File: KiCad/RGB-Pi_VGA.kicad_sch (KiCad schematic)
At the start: 39 parts, among them J1 Raspberry_Pi_4, J2 SCART-F, J3 DE15_Plug_HighDensity_Mountin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, J4 SJ1-3535NG, Q1 MMBT3904, U1 ST662A

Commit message: Change C8, C9 footprints from 1206 to 0805.
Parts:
- C8, C9: footprint Capacitor_SMD:C_1206_3216Metric_Pad1.33x1.80mm_HandSolder -> Resistor_SMD:R_0805_2012Metric_Pad1.20x1.40mm_HandSolder
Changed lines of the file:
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@@
 			)
 		)
-		(property "Footprint" "Capacitor_SMD:C_1206_3216Metric_Pad1.33x1.80mm_HandSolder"
+		(property "Footprint" "Resistor_SMD:R_0805_2012Metric_Pad1.20x1.40mm_HandSolder"
 			(at 228.6 200.9648 0)
 			(hide yes)
@@
 			)
 		)
-		(property "Footprint" "Capacitor_SMD:C_1206_3216Metric_Pad1.33x1.80mm_HandSolder"
+		(property "Footprint" "Resistor_SMD:R_0805_2012Metric_Pad1.20x1.40mm_HandSolder"
 			(at 228.6 195.8848 0)
 			(hide yes)

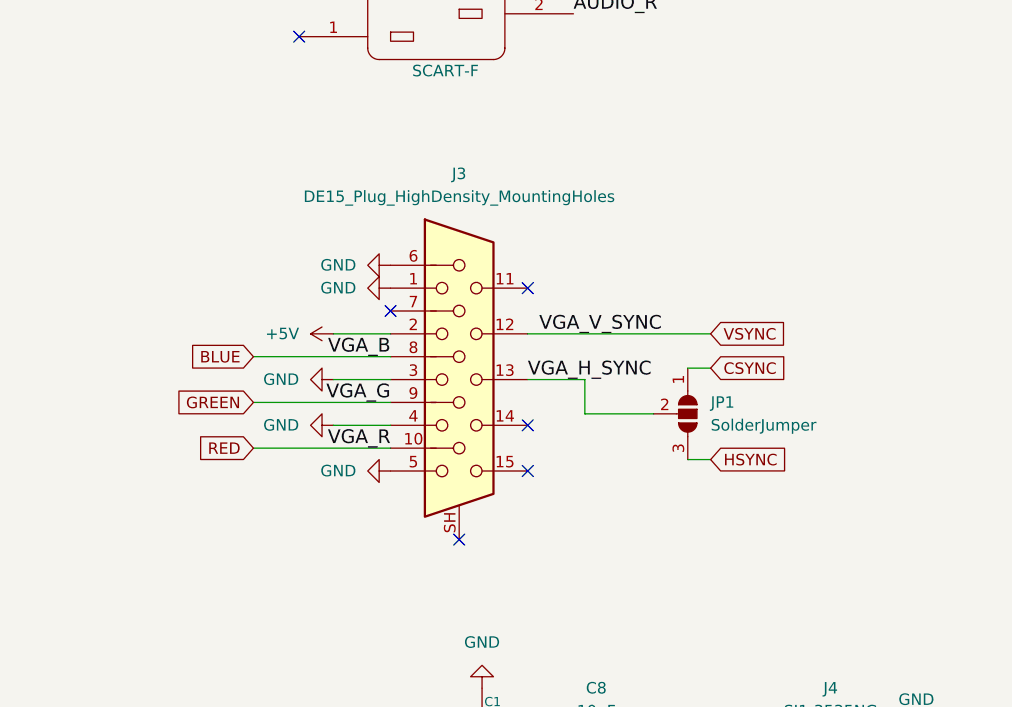
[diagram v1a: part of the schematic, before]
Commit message: Correct DE15/VGA connector pinout.
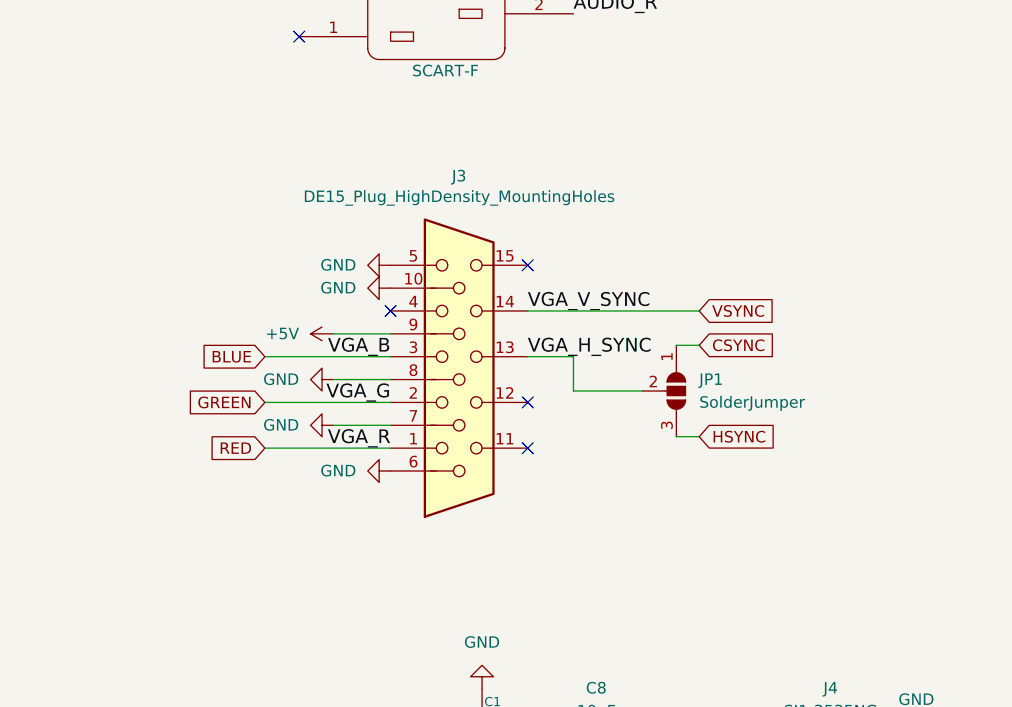
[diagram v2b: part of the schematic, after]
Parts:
- J3: symbol Connector:DE15_Socket_HighDensity_MountingHoles -> Connector:DE15_Socket_HighDensity
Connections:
- net +5V: now also J3.9; no longer J3.2
- net BLUE: now also J3.3; no longer J3.8
- net GND: now also J3.10, J3.7, J3.8; no longer J3.1, J3.3, J3.4
- net GREEN: now also J3.2; no longer J3.9
- net RED: now also J3.1; no longer J3.10
- net VSYNC: now also J3.14; no longer J3.12
- no-connect marks 26 -> 25
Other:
- moved on the sheet: JP1
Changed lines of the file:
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@@
 	)
 	(no_connect
-		(at 209.55 172.72)
-	)
-	(no_connect
 		(at 99.06 129.54)
 	)
@@
 	)
 	(no_connect
-		(at 217.17 144.78)
+		(at 217.17 142.24)
 	)
 	(no_connect
@@
 	)
 	(no_connect
-		(at 217.17 165.1)
+		(at 217.17 162.56)
 	)
 	(no_connect
-		(at 217.17 160.02)
+		(at 217.17 157.48)
 	)
 	(no_connect
@@
 	(wire
 		(pts
+			(xy 217.17 147.32) (xy 236.22 147.32)
+		)
+		(stroke
+			(width 0)
+			(type default)
+		)
+	)
+	(wire
+		(pts
 			(xy 260.35 195.58) (xy 257.81 195.58)
 		)
@@
 	(wire
 		(pts
+			(xy 187.96 152.4) (xy 201.93 152.4)
+		)
+		(stroke
+			(width 0)
+			(type default)
+		)
+	)
+	(wire
+		(pts
 			(xy 54.61 45.72) (xy 58.42 45.72)
 		)
@@
 	(wire
 		(pts
+			(xy 195.58 149.86) (xy 201.93 149.86)
+		)
+		(stroke
+			(width 0)
+			(type default)
+		)
+	)
+	(wire
+		(pts
 			(xy 101.6 41.91) (xy 114.3 41.91)
 		)
@@
 	(wire
 		(pts
+			(xy 187.96 157.48) (xy 201.93 157.48)
+		)
+		(stroke
+			(width 0)
+			(type default)
+		)
+	)
+	(wire
+		(pts
 			(xy 43.18 275.59) (xy 48.26 275.59)
 		)
@@
 	(wire
 		(pts
-			(xy 223.52 154.94) (xy 223.52 158.75)
+			(xy 222.25 152.4) (xy 222.25 156.21)
 		)
 		(stroke
@@
 	(wire
 		(pts
-			(xy 186.69 157.48) (xy 201.93 157.48)
-		)
-		(stroke
-			(width 0)
-			(type default)
-		)
-	)
-	(wire
-		(pts
 			(xy 27.94 182.88) (xy 27.94 184.15)
 		)
@@
 	(wire
 		(pts
-			(xy 237.49 163.83) (xy 234.95 163.83)
+			(xy 236.22 161.29) (xy 233.68 161.29)
 		)
 		(stroke
@@
 	(wire
 		(pts
-			(xy 195.58 160.02) (xy 201.93 160.02)
-		)
-		(stroke
-			(width 0)
-			(type default)
-		)
-	)
-	(wire
-		(pts
 			(xy 130.81 44.45) (xy 137.16 44.45)
 		)
@@
 	(wire
 		(pts
+			(xy 217.17 152.4) (xy 222.25 152.4)
+		)
+		(stroke
+			(width 0)
+			(type default)
+		)
+	)
+	(wire
+		(pts
 			(xy 27.94 228.6) (xy 35.56 228.6)
 		)
@@
 	(wire
 		(pts
-			(xy 195.58 149.86) (xy 201.93 149.86)
-		)
-		(stroke
-			(width 0)
-			(type default)
-		)
-	)
-	(wire
-		(pts
 			(xy 27.94 228.6) (xy 27.94 231.14)
 		)
@@
 	(wire
 		(pts
-			(xy 195.58 154.94) (xy 201.93 154.94)
-		)
-		(stroke
-			(width 0)
-			(type default)
-		)
-	)
-	(wire
-		(pts
 			(xy 176.53 81.28) (xy 191.77 81.28)
 		)
@@
 	(wire
 		(pts
-			(xy 186.69 162.56) (xy 201.93 162.56)
+			(xy 236.22 151.13) (xy 233.68 151.13)
 		)
 		(stroke
@@
 	(wire
 		(pts
-			(xy 237.49 153.67) (xy 234.95 153.67)
+			(xy 63.5 182.88) (xy 67.31 182.88)
 		)
 		(stroke
@@
 	(wire
 		(pts
-			(xy 63.5 182.88) (xy 67.31 182.88)
+			(xy 130.81 46.99) (xy 130.81 52.07)
 		)
 		(stroke
@@
 	(wire
 		(pts
-			(xy 130.81 46.99) (xy 130.81 52.07)
+			(xy 86.36 182.88) (xy 93.98 182.88)
 		)
 		(stroke
@@
 	(wire
 		(pts
-			(xy 86.36 182.88) (xy 93.98 182.88)
+			(xy 127 261.62) (xy 127 264.16)
 		)
 		(stroke
@@
 	(wire
 		(pts
-			(xy 127 261.62) (xy 127 264.16)
+			(xy 48.26 275.59) (xy 54.61 275.59)
 		)
 		(stroke
@@
 	(wire
 		(pts
-			(xy 48.26 275.59) (xy 54.61 275.59)
+			(xy 121.92 228.6) (xy 128.27 228.6)
 		)
 		(stroke
@@
 	(wire
 		(pts
-			(xy 121.92 228.6) (xy 128.27 228.6)
+			(xy 187.96 162.56) (xy 201.93 162.56)
 		)
 		(stroke
@@
 	(wire
 		(pts
-			(xy 186.69 152.4) (xy 201.93 152.4)
+			(xy 195.58 160.02) (xy 201.93 160.02)
 		)
 		(stroke
@@
 	(wire
 		(pts
-			(xy 217.17 154.94) (xy 223.52 154.94)
-		)
-		(stroke
-			(width 0)
-			(type default)
-		)
-	)
-	(wire
-		(pts
 			(xy 176.53 101.6) (xy 191.77 101.6)
 		)
@@
 	(wire
 		(pts
-			(xy 217.17 149.86) (xy 237.49 149.86)
+			(xy 222.25 156.21) (xy 229.87 156.21)
 		)
 		(stroke
@@
 	(wire
 		(pts
-			(xy 223.52 158.75) (xy 231.14 158.75)
+			(xy 27.94 168.91) (xy 27.94 171.45)
 		)
 		(stroke
@@
 	(wire
 		(pts
-			(xy 27.94 168.91) (xy 27.94 171.45)
+			(xy 43.18 31.75) (xy 54.61 31.75)
 		)
 		(stroke
@@
 	(wire
 		(pts
-			(xy 43.18 31.75) (xy 54.61 31.75)
+			(xy 113.03 52.07) (xy 101.6 52.07)
 		)
 		(stroke
@@
 	(wire
 		(pts
-			(xy 113.03 52.07) (xy 101.6 52.07)
+			(xy 195.58 154.94) (xy 201.93 154.94)
 		)
 		(stroke
@@
 	)
 	(label "VGA_H_SYNC"
-		(at 217.17 154.94 0)
+		(at 217.17 152.4 0)
 		(effects
 			(font
@@
 	)
 	(label "VGA_V_SYNC"
-		(at 218.44 149.86 0)
+		(at 217.17 147.32 0)
 		(effects
 			(font
@@
 	(global_label "RED"
 		(shape input)
-		(at 186.69 162.56 180)
+		(at 187.96 162.56 180)
 		(fields_autoplaced yes)
 		(effects
@@
 		)
 		(property "Intersheetrefs" "${INTERSHEET_REFS}"
-			(at 180.0158 162.56 0)
+			(at 181.2858 162.56 0)
 			(hide yes)
 			(show_name no)
@@
 	(global_label "BLUE"
 		(shape input)
-		(at 186.69 152.4 180)
+		(at 187.96 152.4 180)
 		(fields_autoplaced yes)
 		(effects
@@
 		)
 		(property "Intersheetrefs" "${INTERSHEET_REFS}"
-			(at 178.9272 152.4 0)
+			(at 180.1972 152.4 0)
 			(hide yes)
 			(show_name no)
@@
 	(global_label "VSYNC"
 		(shape input)
-		(at 237.49 149.86 0)
+		(at 236.22 147.32 0)
 		(fields_autoplaced yes)
 		(effects
@@
 		)
 		(property "Intersheetrefs" "${INTERSHEET_REFS}"
-			(at 246.4624 149.86 0)
+			(at 245.1924 147.32 0)
 			(hide yes)
 			(show_name no)
@@
 	(global_label "CSYNC"
 		(shape input)
-		(at 237.49 153.67 0)
+		(at 236.22 151.13 0)
 		(fields_autoplaced yes)
 		(effects
@@
 		)
 		(property "Intersheetrefs" "${INTERSHEET_REFS}"
-			(at 246.6438 153.67 0)
+			(at 245.3738 151.13 0)
 			(hide yes)
 			(show_name no)
@@
 	(global_label "HSYNC"
 		(shape input)
-		(at 237.49 163.83 0)
+		(at 236.22 161.29 0)
 		(fields_autoplaced yes)
 		(effects
@@
 		)
 		(property "Intersheetrefs" "${INTERSHEET_REFS}"
-			(at 246.7043 163.83 0)
+			(at 245.4343 161.29 0)
 			(hide yes)
 			(show_name no)
@@
 	(global_label "GREEN"
 		(shape input)
-		(at 186.69 157.48 180)
+		(at 187.96 157.48 180)
 		(fields_autoplaced yes)
 		(effects
@@
 		)
 		(property "Intersheetrefs" "${INTERSHEET_REFS}"
-			(at 177.5363 157.48 0)
+			(at 178.8063 157.48 0)
 			(hide yes)
 			(show_name no)
@@
 	(symbol
 		(lib_id "Jumper:SolderJumper_3_Open")
-		(at 234.95 158.75 270)
+		(at 233.68 156.21 270)
 		(unit 1)
 		(body_style 1)
@@
 		(fields_autoplaced yes)
 		(property "Reference" "JP1"
-			(at 237.49 157.4799 90)
+			(at 236.22 154.9399 90)
 			(show_name no)
 			(do_not_autoplace no)
@@
 		)
 		(property "Value" "SolderJumper"
-			(at 237.49 160.0199 90)
+			(at 236.22 157.4799 90)
 			(show_name no)
 			(do_not_autoplace no)
@@
 		)
 		(property "Footprint" "Jumper:SolderJumper-3_P1.3mm_Open_RoundedPad1.0x1.5mm_NumberLabels"
-			(at 234.95 158.75 0)
+			(at 233.68 156.21 0)
 			(hide yes)
 			(show_name no)
@@
 		)
 		(property "Datasheet" ""
-			(at 219.71 158.75 0)
+			(at 218.44 156.21 0)
 			(hide yes)
 			(show_name no)
@@
 		)
 		(property "Description" "Solder Jumper, 3-pole, open"
-			(at 222.25 158.75 0)
+			(at 220.98 156.21 0)
 			(hide yes)
 			(show_name no)
@@
 		)
 		(property private "KLC_S5.1" "This is a generic symbol, it has fp-filter, but no default footprint"
-			(at 217.17 158.75 0)
+			(at 215.9 156.21 0)
 			(hide yes)
 			(show_name yes)
@@
 		)
 		(property private "KLC_S3.3" "Graphical-Symbol: thickness is 6mm, fill is background"
-			(at 214.63 158.75 0)
+			(at 213.36 156.21 0)
 			(hide yes)
 			(show_name yes)
@@
 	)
 	(symbol
-		(lib_id "Connector:DE15_Socket_HighDensity_MountingHoles")
-		(at 209.55 154.94 0)
+		(lib_id "Connector:DE15_Socket_HighDensity")
+		(at 209.55 152.4 0)
+		(mirror x)
 		(unit 1)
 		(body_style 1)
@@
 		(in_pos_files yes)
 		(dnp no)
-		(fields_autoplaced yes)
 		(property "Reference" "J3"
-			(at 209.55 132.08 0)
+			(at 209.55 132.334 0)
 			(show_name no)
 			(do_not_autoplace no)
@@
 		)
 		(property "Footprint" "Connector_Dsub:DSUB-15-HD_Socket_Horizontal_P2.29x1.90mm_EdgePinOffset3.03mm_Housed_MountingHolesOffset4.94mm"
-			(at 185.42 144.78 0)
+			(at 185.42 162.56 0)
 			(hide yes)
 			(show_name no)
@@
 		)
 		(property "Datasheet" "~"
-			(at 185.42 144.78 0)
+			(at 185.42 162.56 0)
 			(hide yes)
 			(show_name no)
@@
 			)
 		)
-		(property "Description" "15-pin D-SUB connector, socket (female), High density (3 columns), Triple Row, Generic, VGA-connector, Mounting Hole"
-			(at 209.55 154.94 0)
+		(property "Description" "15-pin D-SUB connector, socket (female), High density (3 columns), Triple Row, Generic, VGA-connector"
+			(at 209.55 152.4 0)
 			(hide yes)
 			(show_name no)
@@
 		(pin "10"
 		)
-		(pin "SH"
-		)
 		(pin "5"

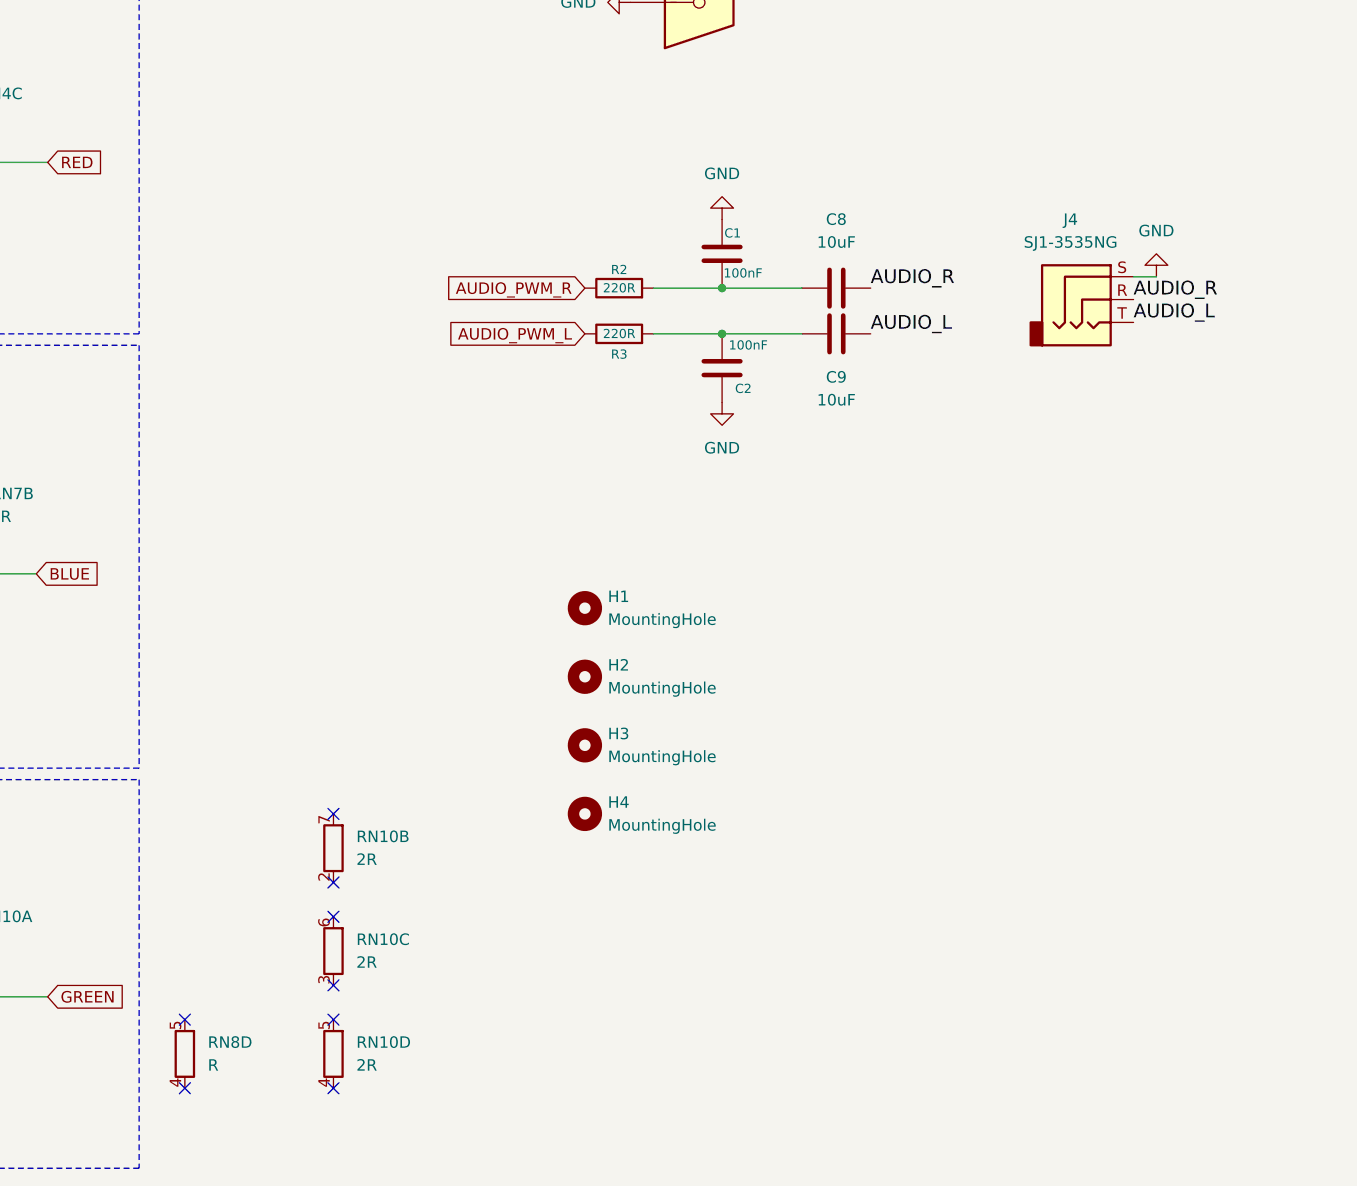
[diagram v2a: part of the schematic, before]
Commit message: Board version 1.1. Correct VGA connector pinout. PWM audio buffered with SN74LVC2G34 Dual Buffer Gate, powered from PS7A2033 Ultra-Low-Noise LDO, with separate analog ground, in order to reduce Raspberry Pi internal power noise. PWM output serial resistors changed from 220R to 1K. Update project description.
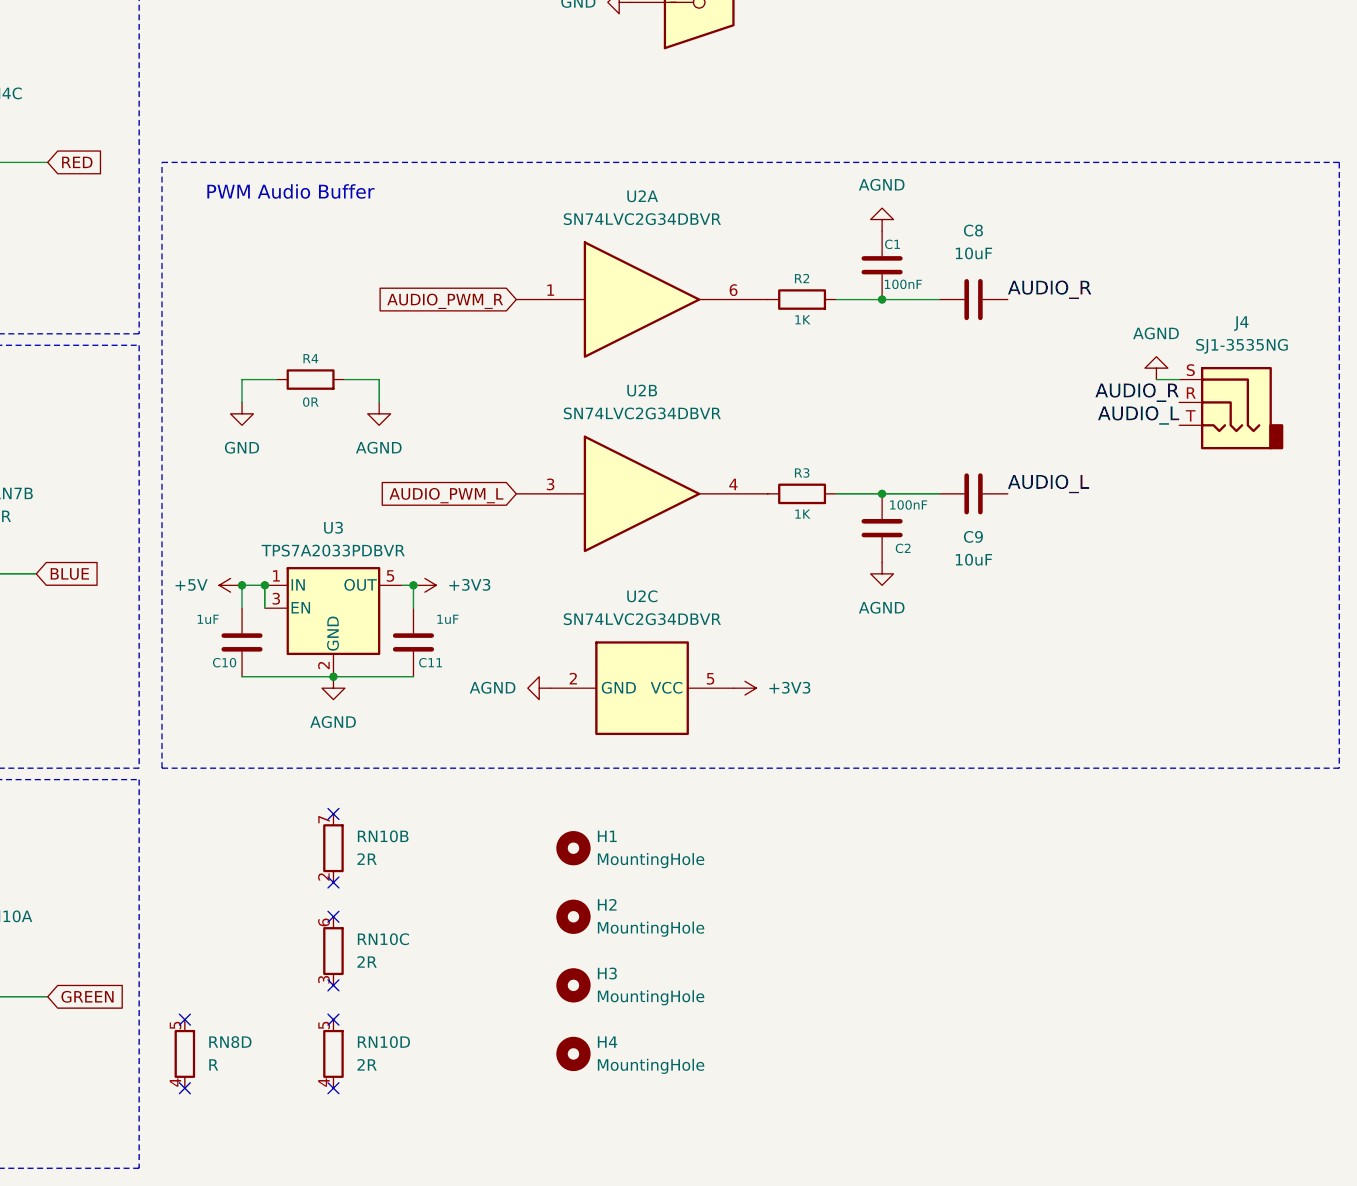
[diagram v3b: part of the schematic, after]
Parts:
- added C10, C11: 1uF, Capacitor_SMD:C_0805_2012Metric_Pad1.18x1.45mm_HandSolder, symbol Device:C
- added R4: 0R, Resistor_SMD:R_0805_2012Metric_Pad1.20x1.40mm_HandSolder, symbol Device:R
- added U2: SN74LVC2G34DBVR, Package_TO_SOT_SMD:SOT-23-6_Handsoldering, symbol 74xGxx:74LVC2G34
- added U3: TPS7A2033PDBVR, Package_TO_SOT_SMD:SOT-23-5, symbol Regulator_Linear:TLV70033_SOT23-5
- R2, R3: value 220R -> 1K
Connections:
- net +5V: now also C10.2, U3.1 (IN), U3.3 (EN)
- net AUDIO_PWM_L: now also U2.3; no longer R3.1
- net AUDIO_PWM_R: now also U2.1; no longer R2.1
- net GND: now also R4.1; no longer C1.1, C2.1, J4.S
- new net: R2.1, U2.6
- new net: R3.1, U2.4
- new net +3V3: C11.2, U2.5 (VCC), U3.5 (OUT)
- new net AGND: C1.1, C10.1, C11.1, C2.1, J4.S, R4.2, U2.2 (GND), U3.2 (GND)
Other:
- note added: "PWM Audio Buffer"
- moved on the sheet: H1, H2, H3, H4
